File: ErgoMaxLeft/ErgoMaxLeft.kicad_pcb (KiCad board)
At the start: 2 copper layers, 92 parts, among them J1 AudioJack4_Ground, K1 KEYSW, K10 KEYSW, K11 KEYSW, K12 KEYSW, K13 KEYSW, K14 KEYSW, K15 KEYSW, K16 KEYSW, K17 KEYSW, K18 KEYSW, K19 KEYSW, K2 KEYSW, K20 KEYSW, K21 KEYSW, K22 KEYSW, K23 KEYSW, K24 KEYSW, K25 KEYSW, K26 KEYSW, K27 KEYSW, K28 KEYSW, K29 KEYSW, K3 KEYSW, K30 KEYSW, K31 KEYSW, K32 KEYSW, K33 KEYSW, K34 KEYSW, K35 KEYSW, K36 KEYSW, K37 KEYSW, K38 KEYSW, K39 KEYSW, K4 KEYSW, K40 KEYSW, K41 KEYSW, K42 KEYSW, K43 KEYSW, K44 KEYSW, K5 KEYSW, K6 KEYSW, K7 KEYSW, K8 KEYSW, K9 KEYSW, U1 ProMicro

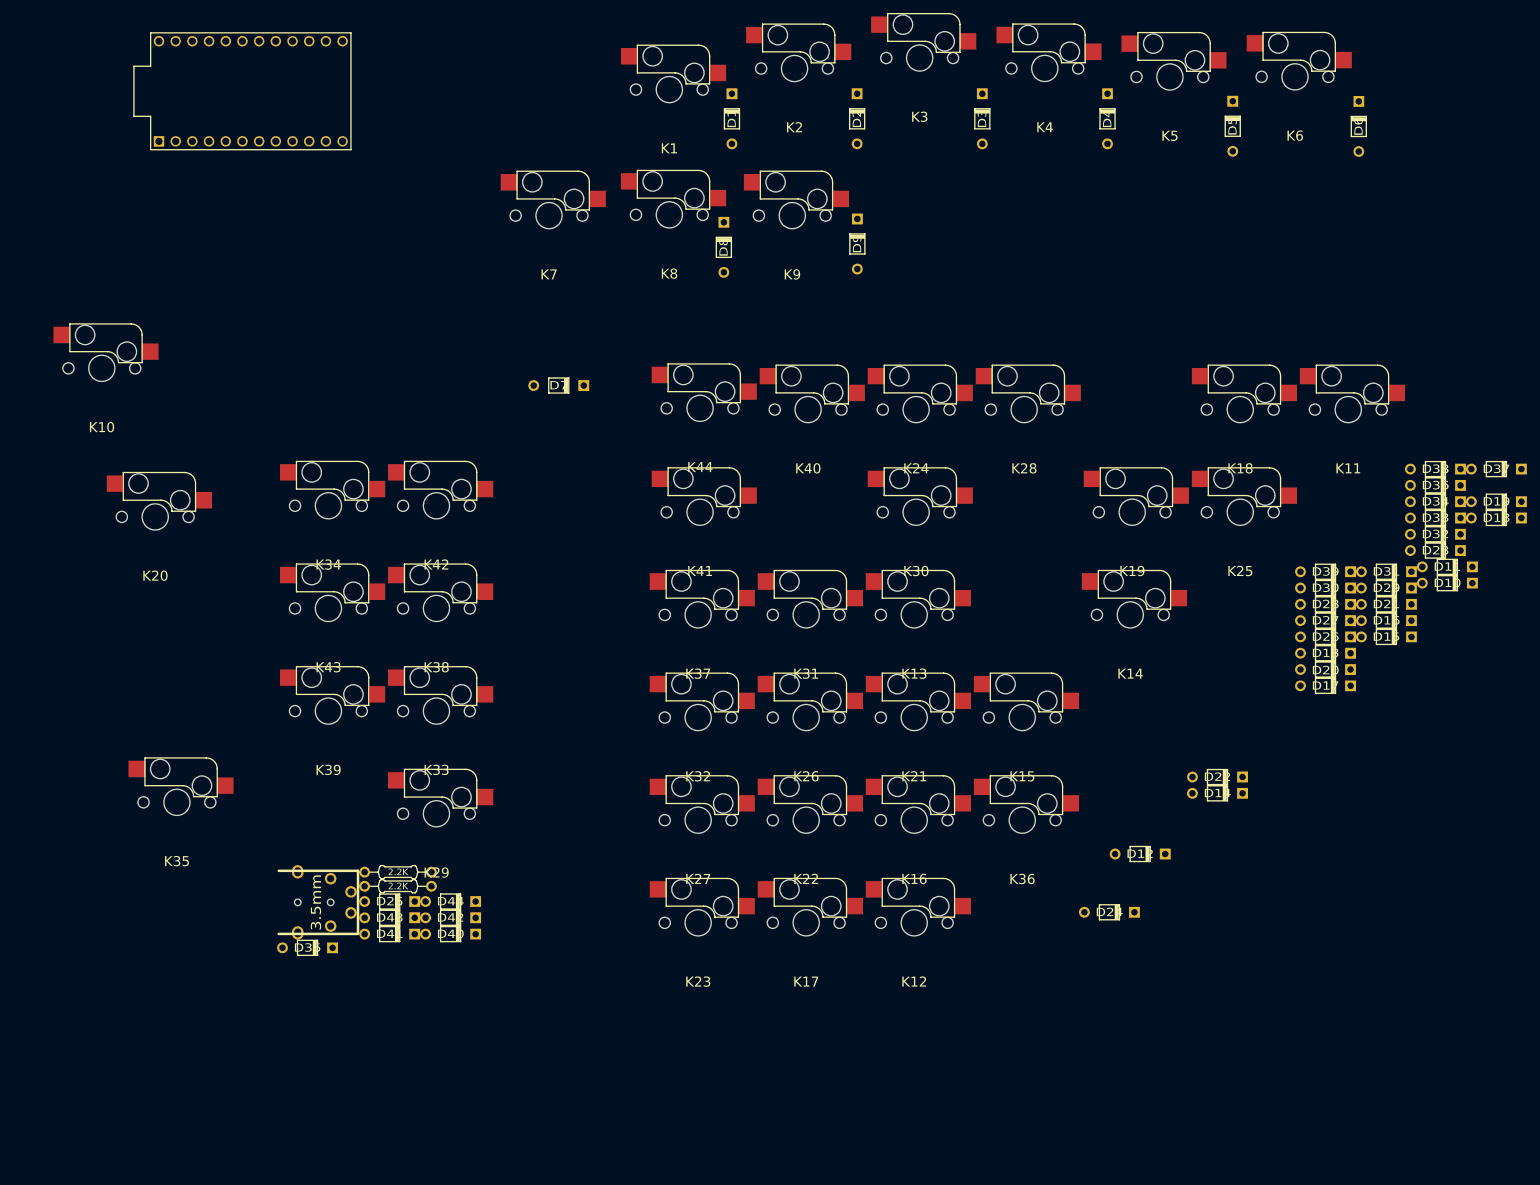
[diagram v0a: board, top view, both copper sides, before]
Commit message: WIP: placing switch sockets on PCB
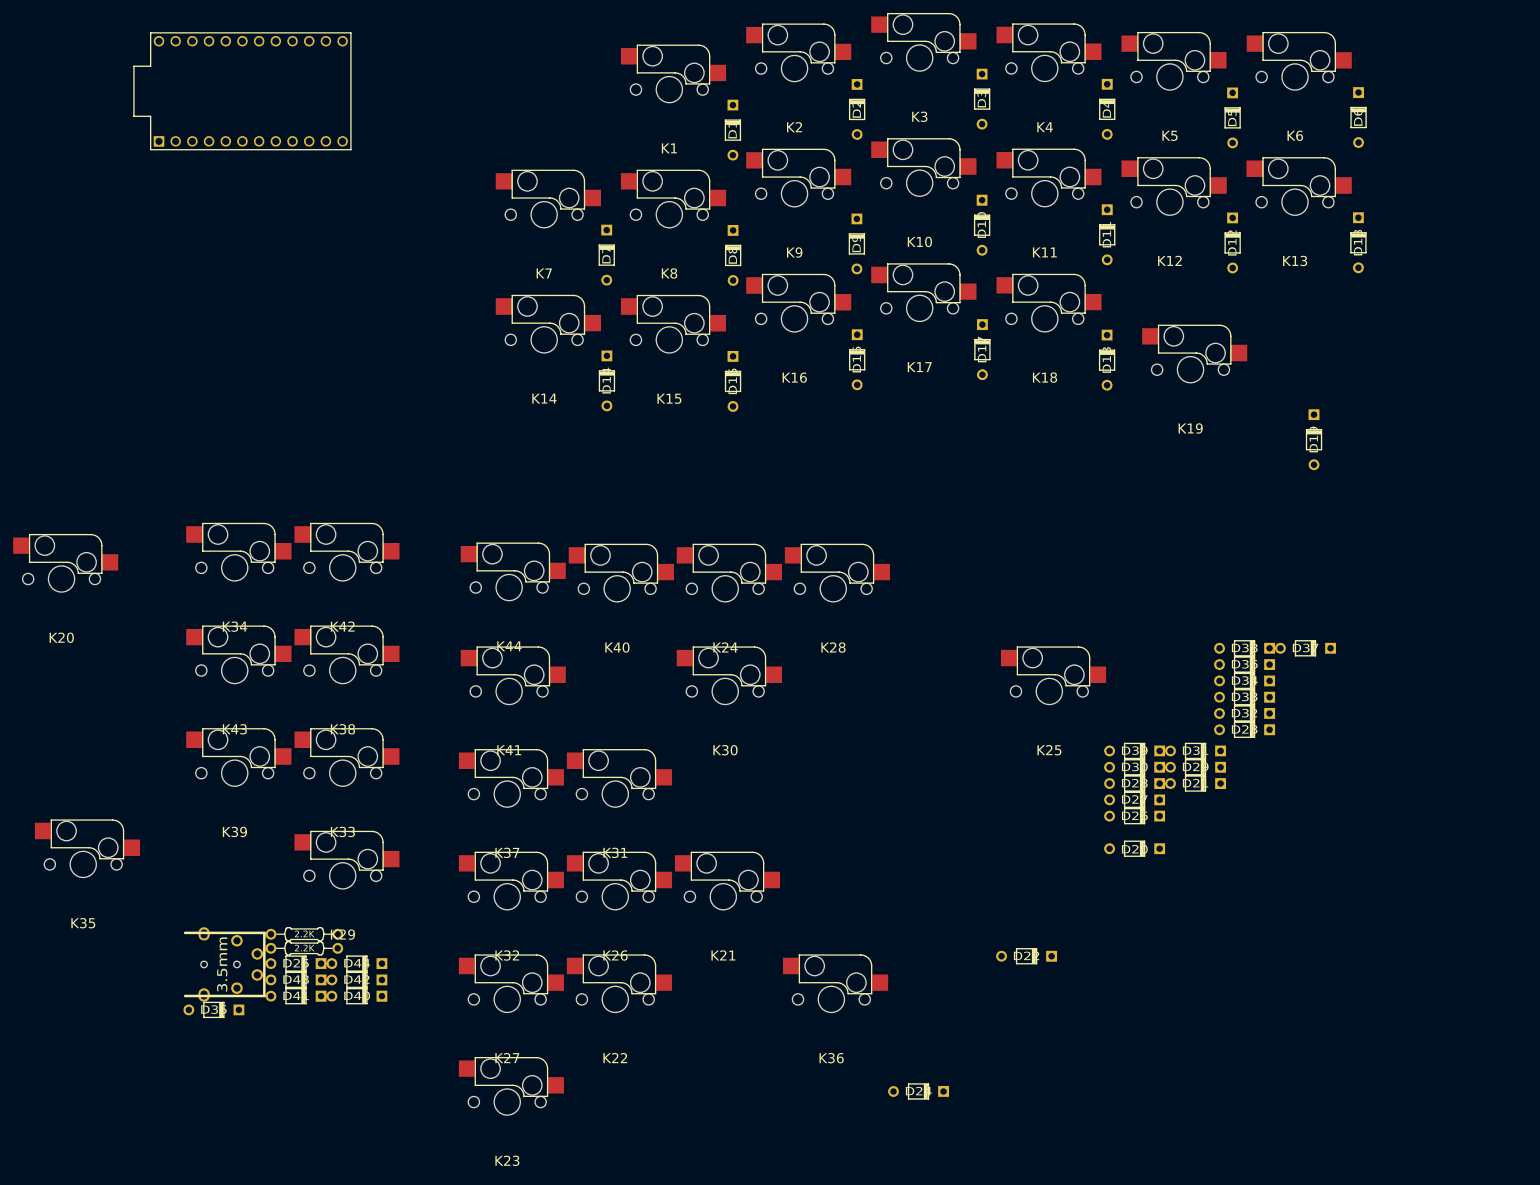
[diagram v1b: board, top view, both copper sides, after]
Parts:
- moved K10 127.6 mm to (165.1, 47.3)
- moved K12 116.4 mm to (203.2, 50.1)
- moved D14 112.1 mm to (117.5, 77.3), turned to 90 degrees
- moved D15 106.8 mm to (136.7, 77.4), turned to 90 degrees
- moved K14 98.5 mm to (108.0, 71.1)
- moved K17 95.1 mm to (165.1, 66.3)
- moved D12 94.0 mm to (212.7, 56.4), turned to 90 degrees
- moved D16 89.8 mm to (155.6, 74.1), turned to 90 degrees
- moved D10 89.3 mm to (174.6, 53.7), turned to 90 degrees
- moved K13 85.4 mm to (222.2, 50.2)
- moved K15 78.7 mm to (127.0, 71.1)
- moved K16 78.4 mm to (146.0, 67.9)
- moved D17 73.1 mm to (174.6, 72.6), turned to 90 degrees
- moved D11 72.3 mm to (193.6, 55.1), turned to 90 degrees
- moved D18 63.9 mm to (193.6, 74.2), turned to 90 degrees
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
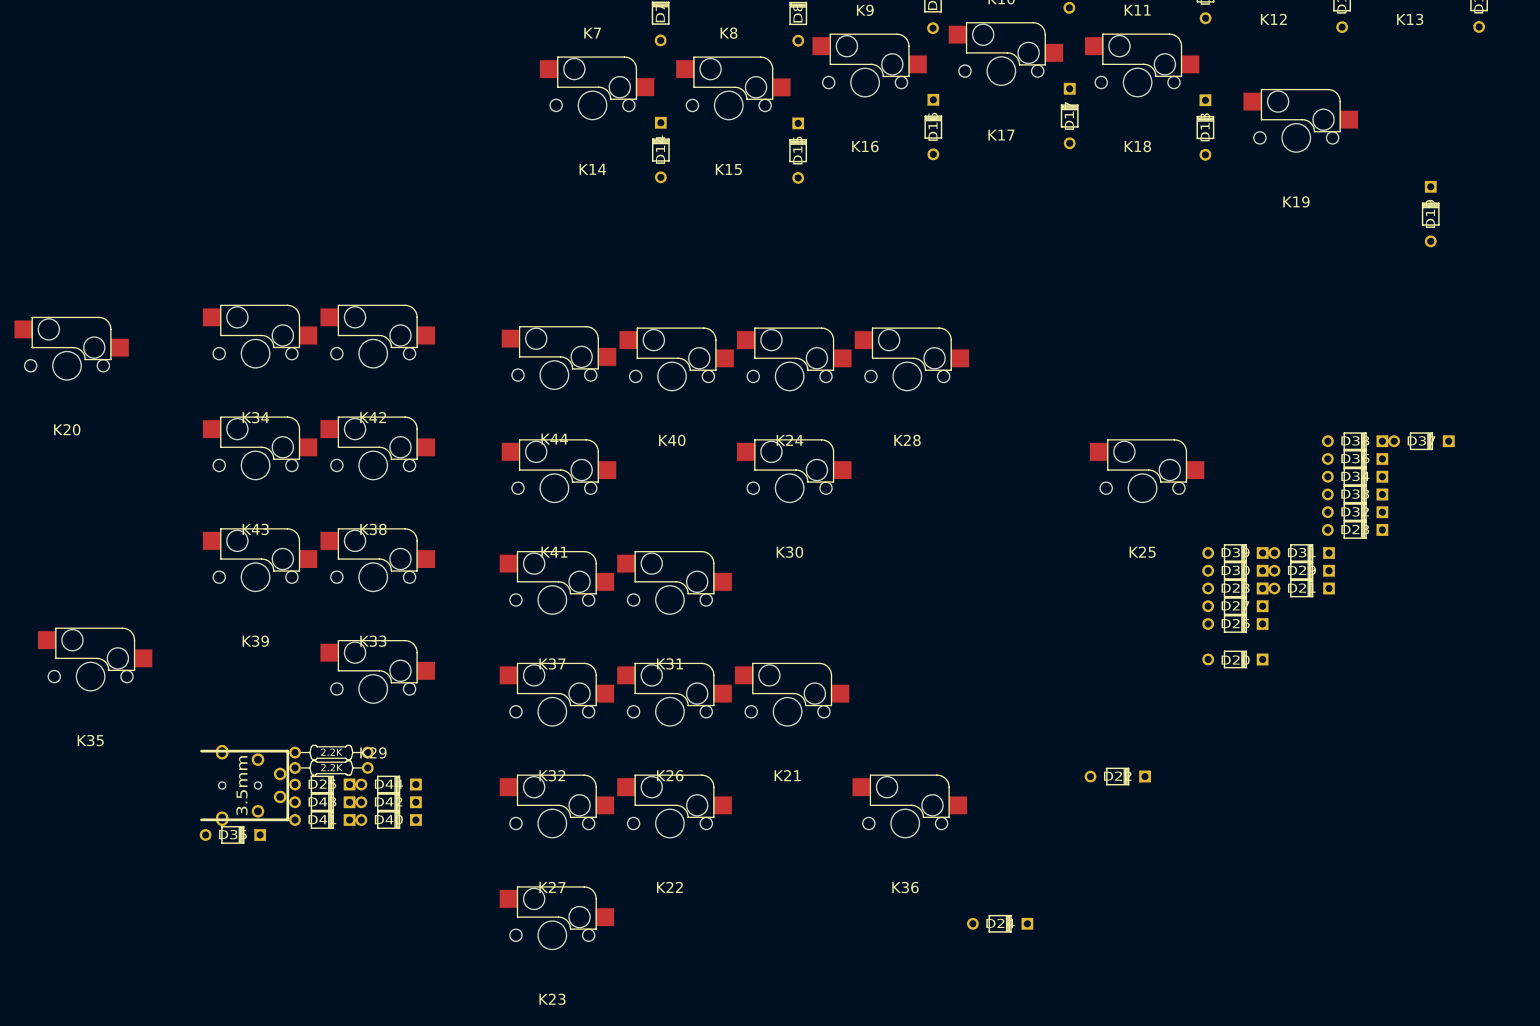
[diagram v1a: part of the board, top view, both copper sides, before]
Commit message: WIP align even more switch sockets, line 4
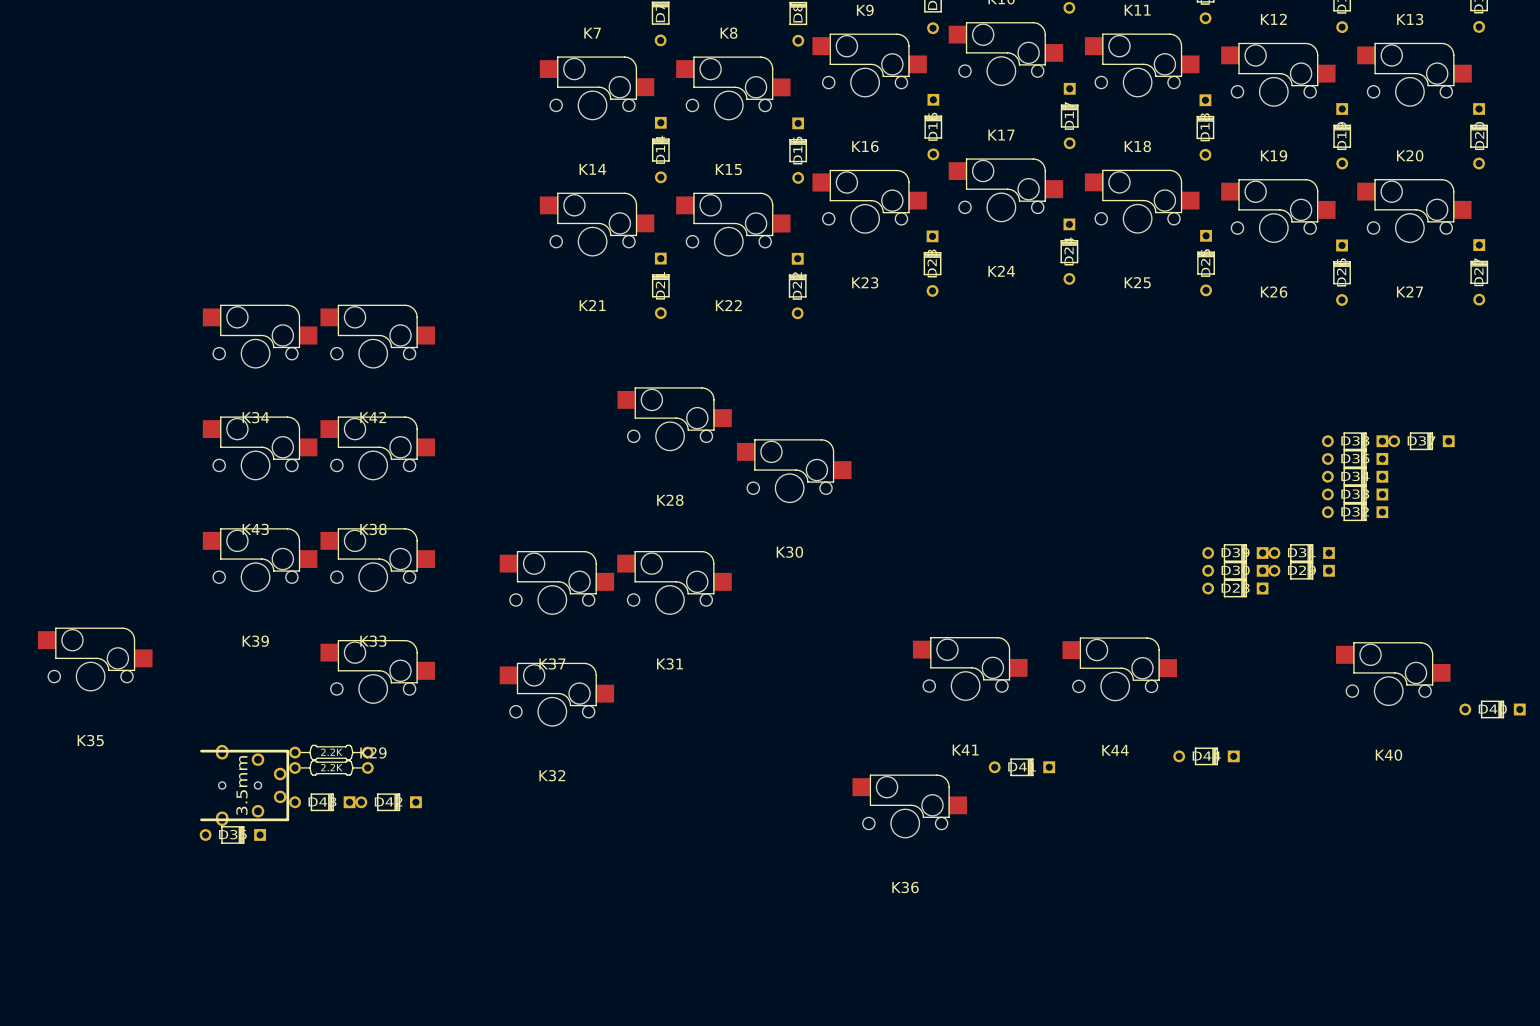
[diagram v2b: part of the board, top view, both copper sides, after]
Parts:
- moved K20 191.5 mm to (222.2, 69.2)
- moved D40 155.0 mm to (233.7, 155.5)
- moved K27 145.9 mm to (222.2, 88.2)
- moved D25 143.4 mm to (193.7, 93.1), turned to 90 degrees
- moved D44 114.4 mm to (193.8, 162.1)
- moved K40 109.4 mm to (219.2, 153.0)
- moved K23 109.3 mm to (146.0, 87.0)
- moved K26 108.1 mm to (203.2, 88.2)
- moved D21 99.1 mm to (117.5, 96.3), turned to 90 degrees
- moved D41 98.1 mm to (168.0, 163.6)
- moved D24 94.4 mm to (174.6, 91.5), turned to 90 degrees
- moved K44 89.6 mm to (181.0, 152.3)
- moved D22 81.9 mm to (136.6, 96.3), turned to 90 degrees
- moved K22 81.7 mm to (127.0, 90.1)
- moved D20 80.7 mm to (231.9, 75.4), turned to 90 degrees
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
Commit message: WIP: PCB - last row set, side keys needed
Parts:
- moved K35 199.1 mm to (230.1, 99.5)
- moved D35 191.6 mm to (239.1, 111.4), turned to 90 degrees
- moved D43 190.8 mm to (260.7, 156.5)
- moved K43 188.8 mm to (246.9, 153.7)
- moved D42 150.7 mm to (227.0, 137.8)
- moved K28 150.4 mm to (268.1, 98.5)
- moved K34 148.8 mm to (209.6, 101.4)
- moved K42 147.5 mm to (223.3, 126.5)
- moved K36 128.4 mm to (269.2, 119.8)
- moved K33 119.1 mm to (190.5, 100.1)
- moved D37 100.6 mm to (123.8, 128.5), turned to 90 degrees
- moved K39 93.3 mm to (152.4, 119.1)
- moved K32 89.8 mm to (171.4, 98.5)
- moved D29 86.9 mm to (123.8, 111.2), turned to 90 degrees
- moved D28 81.8 mm to (270.8, 101.7)
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
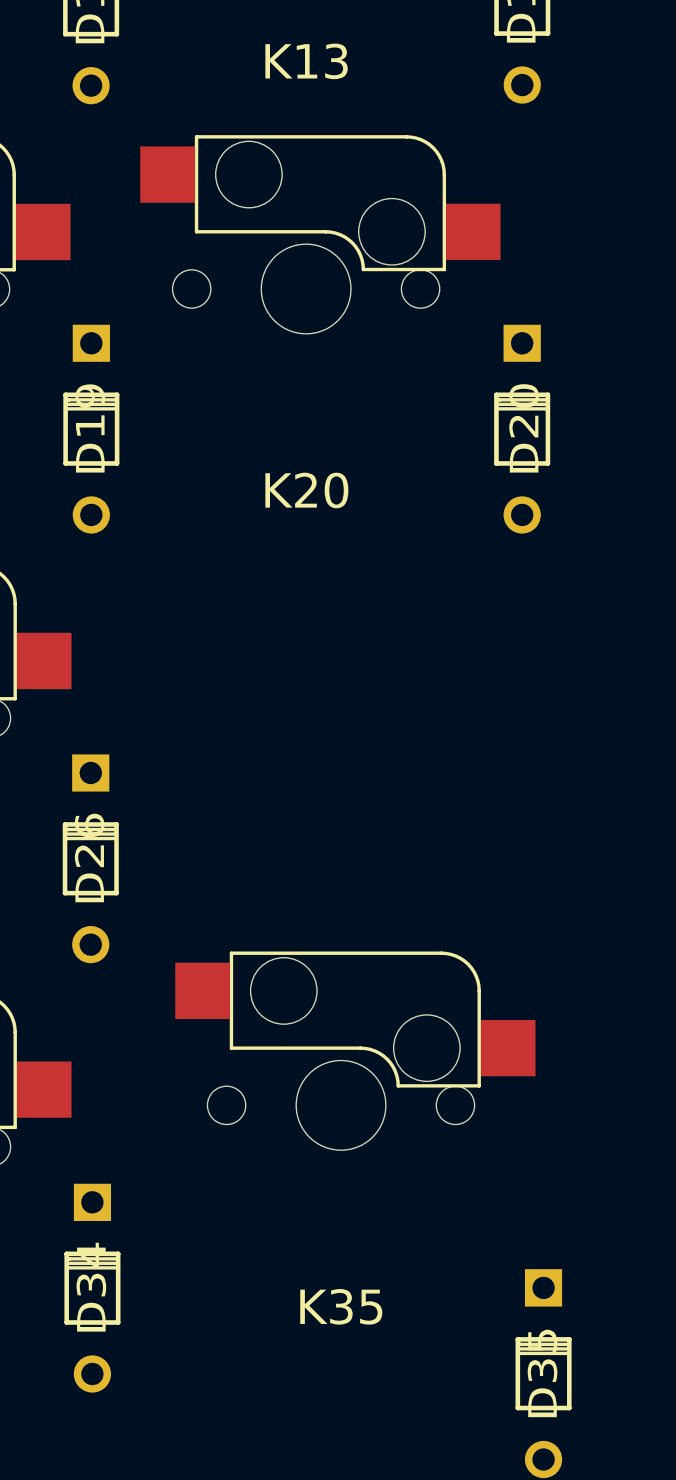
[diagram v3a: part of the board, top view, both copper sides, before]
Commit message: WIP PCB place 2 right side 1.5u key sockets
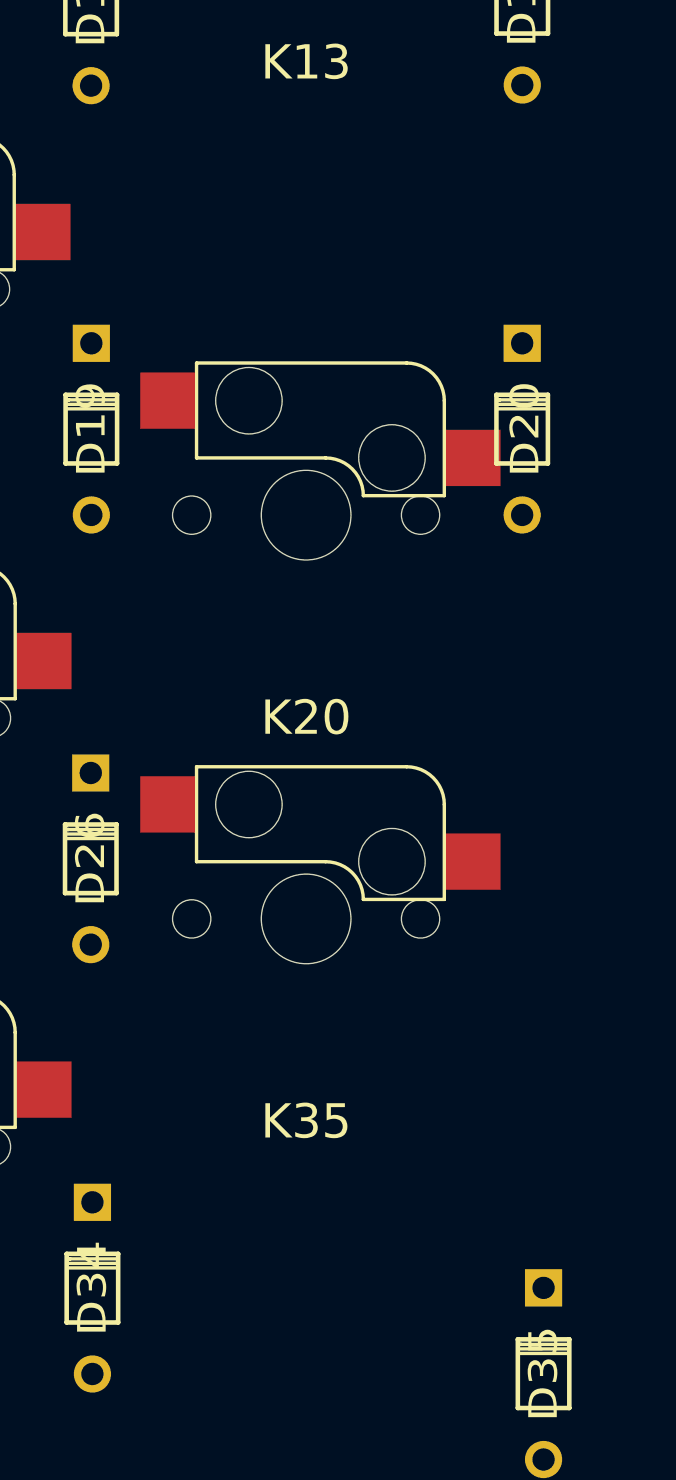
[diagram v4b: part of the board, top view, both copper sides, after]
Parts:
- moved K20 10.0 mm to (228.6, 73.3)
- moved K35 8.42 mm to (228.6, 91.2)
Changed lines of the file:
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@@
-(kicad_pcb (version 20171130) (host pcbnew 5.0.1-33cea8e~68~ubuntu18.04.1)
+(kicad_pcb (version 20171130) (host pcbnew "(5.0.1-3-g963ef8bb5)")
   (general
     (thickness 1.6)
@@
   )
   (module keyboard_parts:Kailh_MX_Socket (layer F.Cu)
-    (at 228.6 63.27564)
+    (at 228.6 73.31564)
     (fp_text reference K20 (at 0 9) (layer F.SilkS)
       (effects (font (size 1.524 1.524) (thickness 0.3048)))
@@
   )
   (module keyboard_parts:Kailh_MX_Socket (layer F.Cu)
-    (at 230.1494 99.5172)
+    (at 228.6 91.24)
     (fp_text reference K35 (at 0 9) (layer F.SilkS)
       (effects (font (size 1.524 1.524) (thickness 0.3048)))

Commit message: WIP PCB - place left 1.5u switch sockets
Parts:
- moved K14 4.76 mm to (109.5, 65.2)
- moved K21 4.76 mm to (109.5, 84.2)
- moved K7 4.76 mm to (109.5, 46.1)
- moved K29 4.76 mm to (109.5, 103.3)
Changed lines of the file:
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@@
-(kicad_pcb (version 20171130) (host pcbnew "(5.0.1-3-g963ef8bb5)")
+(kicad_pcb (version 20171130) (host pcbnew "(5.0.1)-3")
   (general
     (thickness 1.6)
@@
     (solder_mask_min_width 0.25)
     (aux_axis_origin 0 0)
-    (visible_elements FFFFF77F)
+    (visible_elements 7FFFF7FF)
     (pcbplotparams
       (layerselection 0x010fc_ffffffff)
@@
   )
   (module keyboard_parts:Kailh_MX_Socket locked (layer F.Cu)
-    (at 114.29168 46.14064)
+    (at 109.53168 46.14064)
     (fp_text reference K7 (at 0 9) (layer F.SilkS)
       (effects (font (size 1.524 1.524) (thickness 0.3048)))
@@
   )
   (module keyboard_parts:Kailh_MX_Socket locked (layer F.Cu)
-    (at 114.29508 65.18374)
+    (at 109.53508 65.18374)
     (fp_text reference K14 (at 0 9) (layer F.SilkS)
       (effects (font (size 1.524 1.524) (thickness 0.3048)))
@@
   )
   (module keyboard_parts:Kailh_MX_Socket (layer F.Cu)
-    (at 114.3054 84.22384)
+    (at 109.5454 84.22384)
     (fp_text reference K21 (at 0 9) (layer F.SilkS)
       (effects (font (size 1.524 1.524) (thickness 0.3048)))
@@
   )
   (module keyboard_parts:Kailh_MX_Socket (layer F.Cu)
-    (at 114.3 103.27)
+    (at 109.54 103.27)
     (fp_text reference K29 (at 0 9) (layer F.SilkS)
       (effects (font (size 1.524 1.524) (thickness 0.3048)))
